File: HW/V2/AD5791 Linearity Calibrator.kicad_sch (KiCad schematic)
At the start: 56 parts, among them J11 ISO OUT, J11 PWR, J2 VREFP, J3 VREFN, J5 VREFP, SW1 RST, U1 LM317, U12 ADuM1201AR, U2 AD5791BRUZ, U2 LM337, U3 ADR1399, U3 LM317, U6 REFSCALE, U7 REFBUF, U8 Pico, U9 OUTBUF

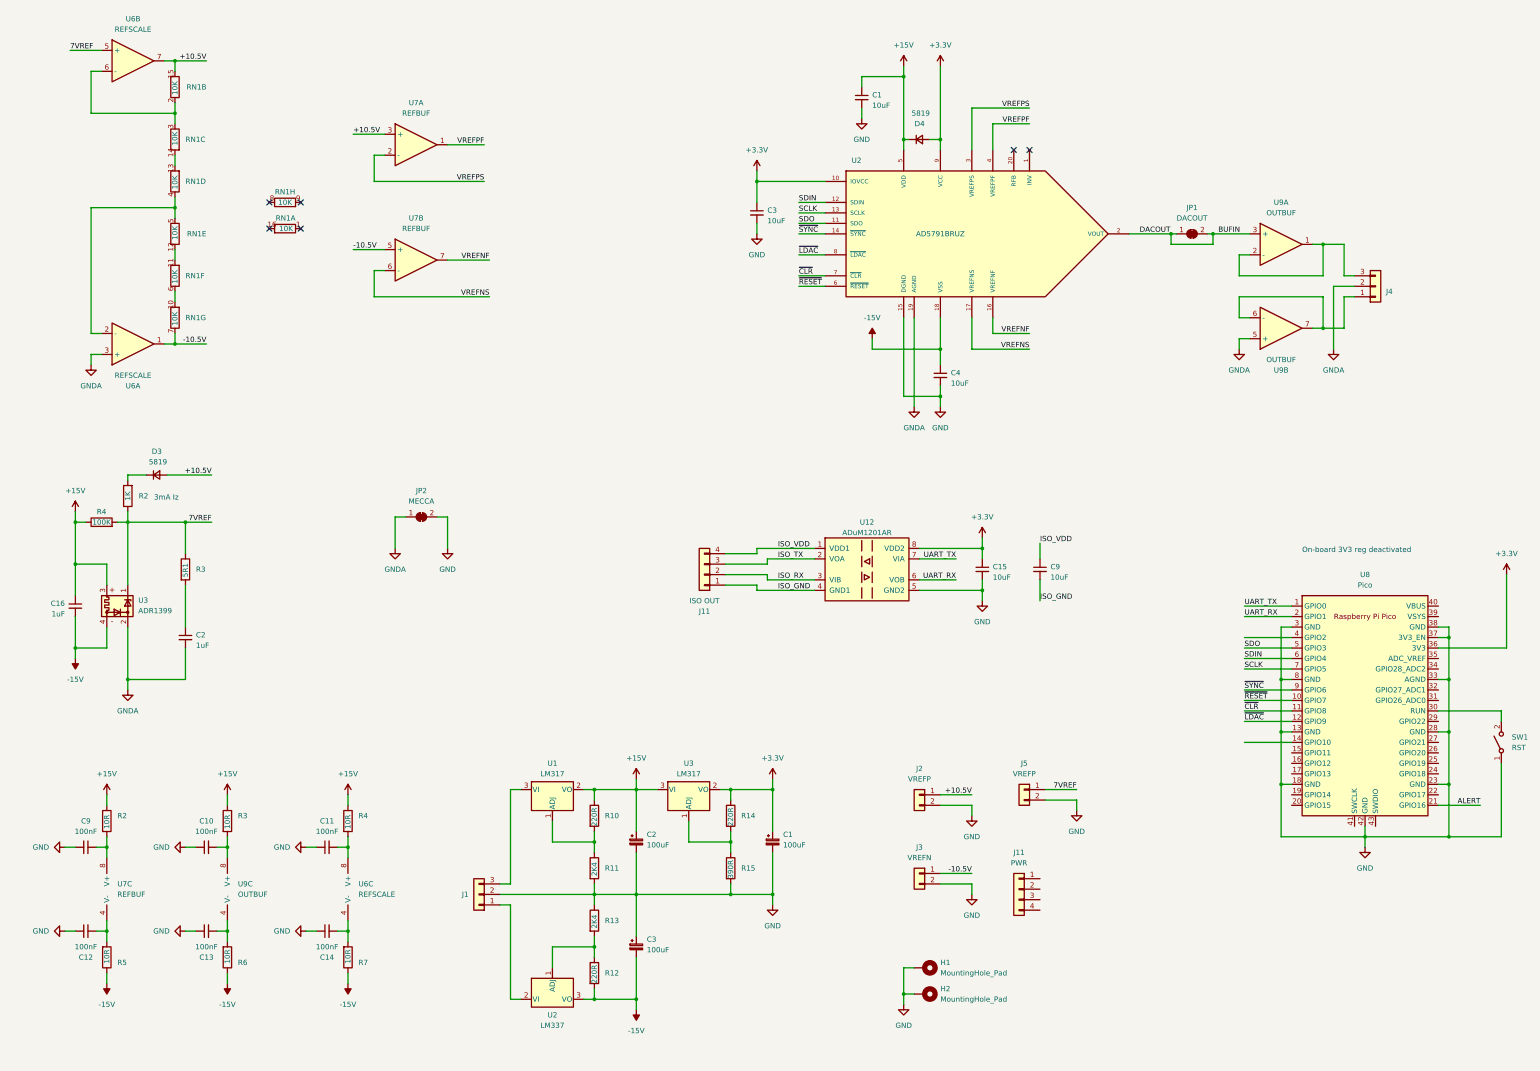
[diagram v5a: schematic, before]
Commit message: updated layout
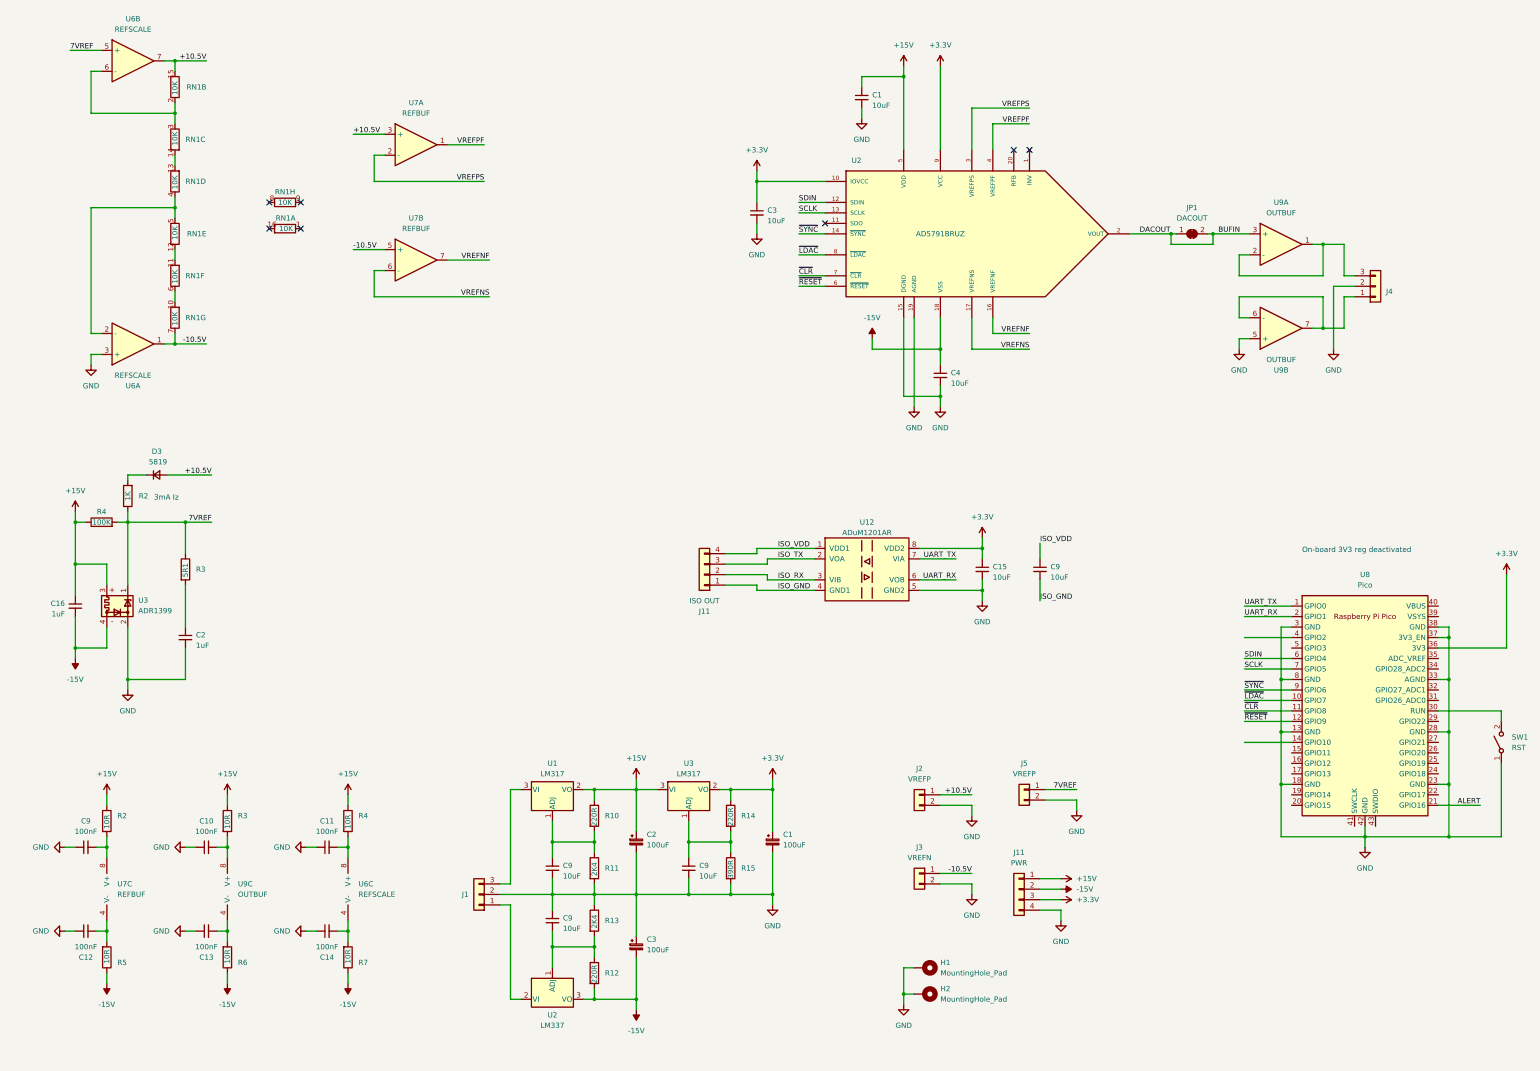
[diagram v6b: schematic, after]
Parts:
- removed D4: 5819, Resistor_SMD:R_0603_1608Metric_Pad0.98x0.95mm_HandSolder, symbol Device:D_Small
- removed JP2: MECCA, Connector_PinHeader_1.27mm:PinHeader_1x02_P1.27mm_Vertical, symbol Jumper:SolderJumper_2_Bridged
- added C9 (x3): 10uF, Resistor_SMD:R_0603_1608Metric, symbol Device:C_Small
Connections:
- net GNDA is gone; now on net GND: C2.2, J4.2 (Pin_2), U2.19 (AGND), U3.2, U6.3 (+), U9.5 (+)
- net +15V: now also J11.1 (Pin_1)
- net +3.3V: now also J11.3 (Pin_3)
- net -15V: now also J11.2 (Pin_2)
- net GND: now also J11.4 (Pin_4), C9.1, C9.2, C9.2
- net ~{LDAC}: now also U8.10 (GPIO7); no longer U8.12 (GPIO9)
- net ~{RESET}: now also U8.12 (GPIO9); no longer U8.10 (GPIO7)
- net at R14.2, R15.1, U3.1 (ADJ): now also C9.1
- net at R12.1, R13.2, U2.1 (ADJ): now also C9.2
- net at R10.2, R11.1, U1.1 (ADJ): now also C9.1
- net SDO: no longer names the net of U8.5 (GPIO3)
- net SDO: no longer U2.11 (SDO)
- no-connect marks 6 -> 7

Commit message: updated files
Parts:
- added U11: ADuM1400xRW, Package_SO:SOIC-16W_7.5x10.3mm_P1.27mm, symbol Isolator:ADuM1400xRW
- added U12: ISO7340C, Package_SO:SOIC-16W_7.5x10.3mm_P1.27mm, symbol Isolator:ISO7340C
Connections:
- net +10.5V: now also U7.5 (+); no longer U7.3 (+)
- net +15V: now also J11.2 (Pin_2); no longer J11.1 (Pin_1)
- net -10.5V: now also U7.3 (+); no longer U7.5 (+)
- net -15V: now also J11.1 (Pin_1); no longer J11.2 (Pin_2)
- net VREFNF: now also U7.1; no longer U7.7
- net VREFNS: now also U7.2 (-); no longer U7.6 (-)
- net VREFPF: now also U7.7; no longer U7.1
- net VREFPS: now also U7.6 (-); no longer U7.2 (-)
- new net: U12.15 (GND2), U12.9 (GND2)
- new net: U12.2 (GND1), U12.8 (GND1)
- new net: U11.15 (GND2), U11.9 (GND2)
- new net: U11.2 (GND1), U11.8 (GND1)
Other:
- moved on the sheet: U7A, U7B
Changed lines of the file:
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@@
+    )
+  )
+  (symbol (lib_id "Isolator:ISO7340C") (at 119.38 135.89 0) (unit 1)
+    (in_bom yes) (on_board yes) (dnp no) (fields_autoplaced)
+    (property "Reference" "U12" (at 119.38 118.11 0)
+      (effects (font (size 1.27 1.27)))
+    )
+    (property "Value" "ISO7340C" (at 119.38 120.65 0)
+      (effects (font (size 1.27 1.27)))
+    )
+    (property "Footprint" "Package_SO:SOIC-16W_7.5x10.3mm_P1.27mm" (at 119.38 149.86 0)
+      (effects (font (size 1.27 1.27) italic) hide)
+    )
+    (property "Datasheet" "http://www.ti.com/general/docs/lit/getliterature.tsp?genericPartNumber=iso7340c&fileType=pdf" (at 119.38 125.73 0)
+      (effects (font (size 1.27 1.27)) hide)
+    )
+    (pin "1")
+    (pin "10")
+    (pin "11")
+    (pin "12")
+    (pin "13")
+    (pin "14")
+    (pin "15")
+    (pin "16")
+    (pin "2")
+    (pin "3")
+    (pin "4")
+    (pin "5")
+    (pin "6")
+    (pin "8")
+    (pin "9")
+    (instances
+      (project "AD5791 Linearity Calibrator"
+        (path "/e4c8fe5c-4d6c-45a9-911b-05eafd37681e"
+          (reference "U12") (unit 1)
+        )
+      )
     )
   )
@@
     )
   )
-  (symbol (lib_id "power:+15V") (at 278.13 233.68 270) (unit 1)
-    (in_bom yes) (on_board yes) (dnp no) (fields_autoplaced)
-    (property "Reference" "#PWR034" (at 274.32 233.68 0)
-      (effects (font (size 1.27 1.27)) hide)
-    )
-    (property "Value" "+15V" (at 281.94 233.68 90)
-      (effects (font (size 1.27 1.27)) (justify left))
-    )
-    (property "Footprint" "" (at 278.13 233.68 0)
-      (effects (font (size 1.27 1.27)) hide)
-    )
-    (property "Datasheet" "" (at 278.13 233.68 0)
+  (symbol (lib_id "power:+15V") (at 278.13 236.22 270) (unit 1)
+    (in_bom yes) (on_board yes) (dnp no) (fields_autoplaced)
+    (property "Reference" "#PWR034" (at 274.32 236.22 0)
+      (effects (font (size 1.27 1.27)) hide)
+    )
+    (property "Value" "+15V" (at 281.94 236.22 90)
+      (effects (font (size 1.27 1.27)) (justify left))
+    )
+    (property "Footprint" "" (at 278.13 236.22 0)
+      (effects (font (size 1.27 1.27)) hide)
+    )
+    (property "Datasheet" "" (at 278.13 236.22 0)
       (effects (font (size 1.27 1.27)) hide)
     )
@@
     )
   )
-  (symbol (lib_id "Device:Opamp_Dual") (at 121.92 83.82 0) (unit 2)
-    (in_bom yes) (on_board yes) (dnp no) (fields_autoplaced)
-    (property "Reference" "U7" (at 121.92 73.66 0)
-      (effects (font (size 1.27 1.27)))
-    )
-    (property "Value" "REFBUF" (at 121.92 76.2 0)
-      (effects (font (size 1.27 1.27)))
-    )
-    (property "Footprint" "Package_SO:SOIC-8_3.9x4.9mm_P1.27mm" (at 121.92 83.82 0)
-      (effects (font (size 1.27 1.27)) hide)
-    )
-    (property "Datasheet" "~" (at 121.92 83.82 0)
+  (symbol (lib_id "Device:Opamp_Dual") (at 121.92 55.88 0) (unit 2)
+    (in_bom yes) (on_board yes) (dnp no) (fields_autoplaced)
+    (property "Reference" "U7" (at 121.92 45.72 0)
+      (effects (font (size 1.27 1.27)))
+    )
+    (property "Value" "REFBUF" (at 121.92 48.26 0)
+      (effects (font (size 1.27 1.27)))
+    )
+    (property "Footprint" "Package_SO:SOIC-8_3.9x4.9mm_P1.27mm" (at 121.92 55.88 0)
+      (effects (font (size 1.27 1.27)) hide)
+    )
+    (property "Datasheet" "~" (at 121.92 55.88 0)
       (effects (font (size 1.27 1.27)) hide)
     )
@@
     )
   )
-  (symbol (lib_id "Device:Opamp_Dual") (at 121.92 55.88 0) (unit 1)
-    (in_bom yes) (on_board yes) (dnp no) (fields_autoplaced)
-    (property "Reference" "U7" (at 121.92 45.72 0)
-      (effects (font (size 1.27 1.27)))
-    )
-    (property "Value" "REFBUF" (at 121.92 48.26 0)
-      (effects (font (size 1.27 1.27)))
-    )
-    (property "Footprint" "Package_SO:SOIC-8_3.9x4.9mm_P1.27mm" (at 121.92 55.88 0)
-      (effects (font (size 1.27 1.27)) hide)
-    )
-    (property "Datasheet" "~" (at 121.92 55.88 0)
+  (symbol (lib_id "Device:Opamp_Dual") (at 121.92 83.82 0) (unit 1)
+    (in_bom yes) (on_board yes) (dnp no) (fields_autoplaced)
+    (property "Reference" "U7" (at 121.92 73.66 0)
+      (effects (font (size 1.27 1.27)))
+    )
+    (property "Value" "REFBUF" (at 121.92 76.2 0)
+      (effects (font (size 1.27 1.27)))
+    )
+    (property "Footprint" "Package_SO:SOIC-8_3.9x4.9mm_P1.27mm" (at 121.92 83.82 0)
+      (effects (font (size 1.27 1.27)) hide)
+    )
+    (property "Datasheet" "~" (at 121.92 83.82 0)
       (effects (font (size 1.27 1.27)) hide)
     )
@@
     )
   )
-  (symbol (lib_id "power:-15V") (at 278.13 236.22 270) (unit 1)
-    (in_bom yes) (on_board yes) (dnp no) (fields_autoplaced)
-    (property "Reference" "#PWR033" (at 280.67 236.22 0)
-      (effects (font (size 1.27 1.27)) hide)
-    )
-    (property "Value" "-15V" (at 281.94 236.22 90)
-      (effects (font (size 1.27 1.27)) (justify left))
-    )
-    (property "Footprint" "" (at 278.13 236.22 0)
-      (effects (font (size 1.27 1.27)) hide)
-    )
-    (property "Datasheet" "" (at 278.13 236.22 0)
-      (effects (font (size 1.27 1.27)) hide)
-    )
+  (symbol (lib_id "Isolator:ADuM1400xRW") (at 156.21 135.89 0) (unit 1)
+    (in_bom yes) (on_board yes) (dnp no) (fields_autoplaced)
+    (property "Reference" "U11" (at 156.21 115.57 0)
+      (effects (font (size 1.27 1.27)))
+    )
+    (property "Value" "ADuM1400xRW" (at 156.21 118.11 0)
+      (effects (font (size 1.27 1.27)))
+    )
+    (property "Footprint" "Package_SO:SOIC-16W_7.5x10.3mm_P1.27mm" (at 156.21 150.495 0)
+      (effects (font (size 1.27 1.27)) hide)
+    )
+    (property "Datasheet" "https://www.analog.com/media/en/technical-documentation/data-sheets/ADUM1400_1401_1402.pdf" (at 135.89 135.89 0)
+      (effects (font (size 1.27 1.27)) hide)
+    )
+    (pin "1")
+    (pin "10")
+    (pin "11")
+    (pin "12")
+    (pin "13")
+    (pin "14")
+    (pin "15")
+    (pin "16")
+    (pin "2")
+    (pin "3")
+    (pin "4")
+    (pin "5")
+    (pin "6")
+    (pin "7")
+    (pin "8")
+    (pin "9")
+    (instances
+      (project "AD5791 Linearity Calibrator"
+        (path "/e4c8fe5c-4d6c-45a9-911b-05eafd37681e"
+          (reference "U11") (unit 1)
+        )
+      )
+    )
+  )
+  (symbol (lib_id "power:-15V") (at 278.13 233.68 270) (unit 1)
+    (in_bom yes) (on_board yes) (dnp no) (fields_autoplaced)
+    (property "Reference" "#PWR033" (at 280.67 233.68 0)
+      (effects (font (size 1.27 1.27)) hide)
+    )
+    (property "Value" "-15V" (at 281.94 233.68 90)
+      (effects (font (size 1.27 1.27)) (justify left))
+    )
+    (property "Footprint" "" (at 278.13 233.68 0)
+      (effects (font (size 1.27 1.27)) hide)
+    )
+    (property "Datasheet" "" (at 278.13 233.68 0)
+      (effects (font (size 1.27 1.27)) hide)
+    )
